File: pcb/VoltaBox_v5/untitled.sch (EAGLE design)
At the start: 46 parts, among them J1 1050170001, Q1 8 MHz, Q2 32768Hz, U1 MCU-STM32F103RCT6(LQFP64), U2 ADUM1401WTRWZ, U4 LMP92064SD/NOPB, X1 112J-TDAR-R(MICROSD)

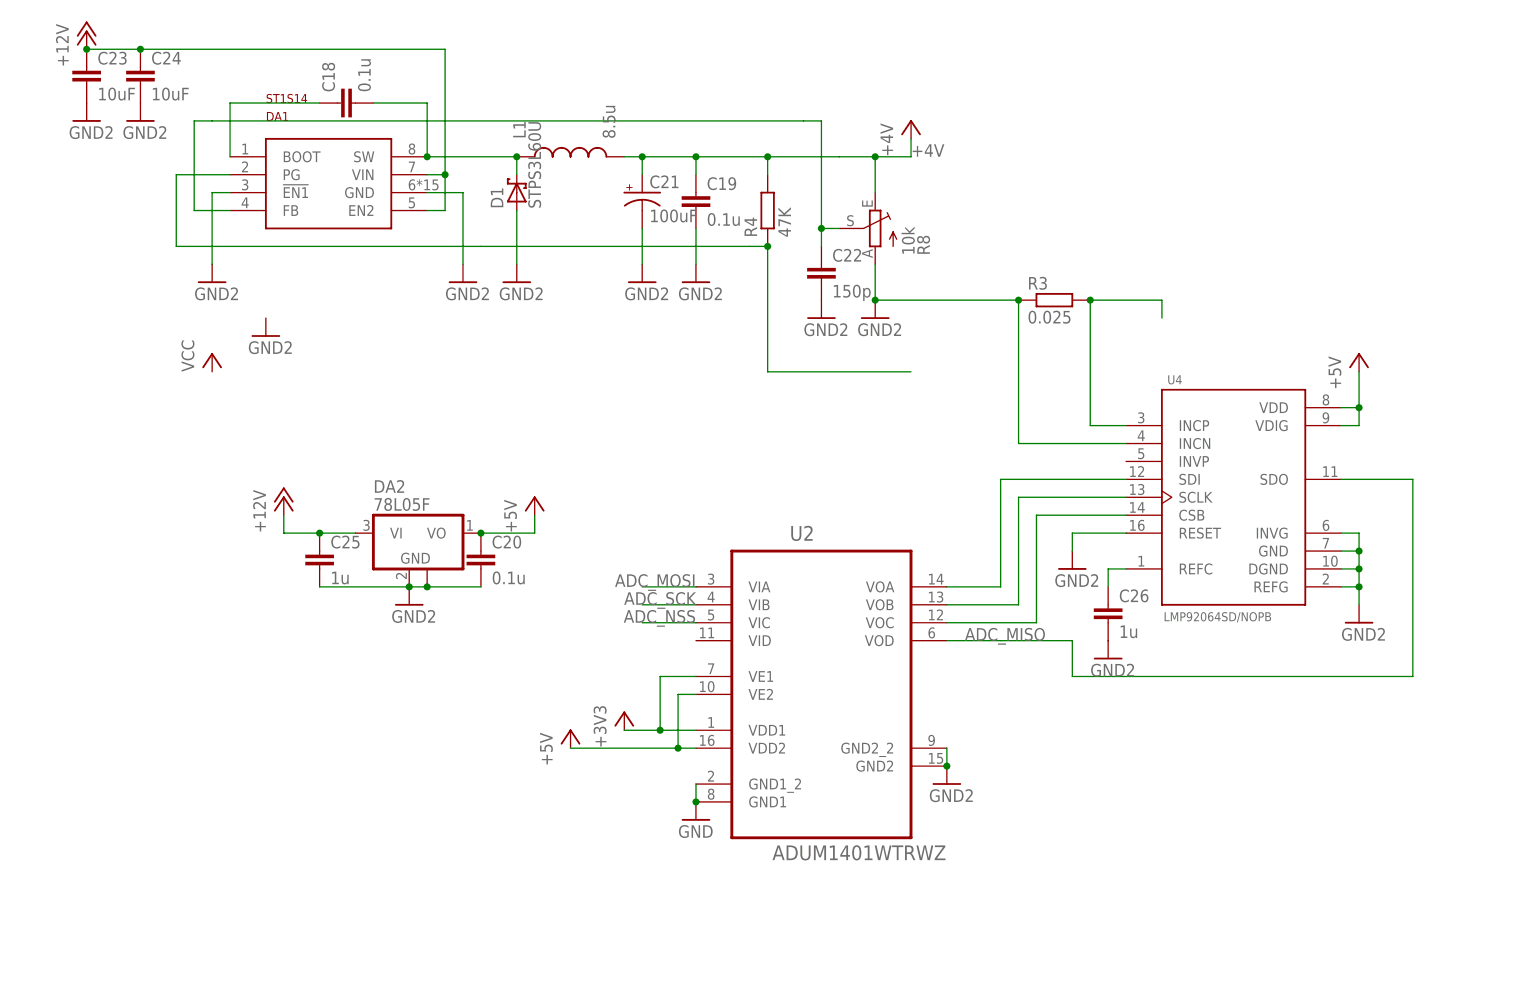
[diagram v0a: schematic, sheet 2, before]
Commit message: Some PCB changes. ICs prefix changes. Added some capacitors. Q3 case type changed.
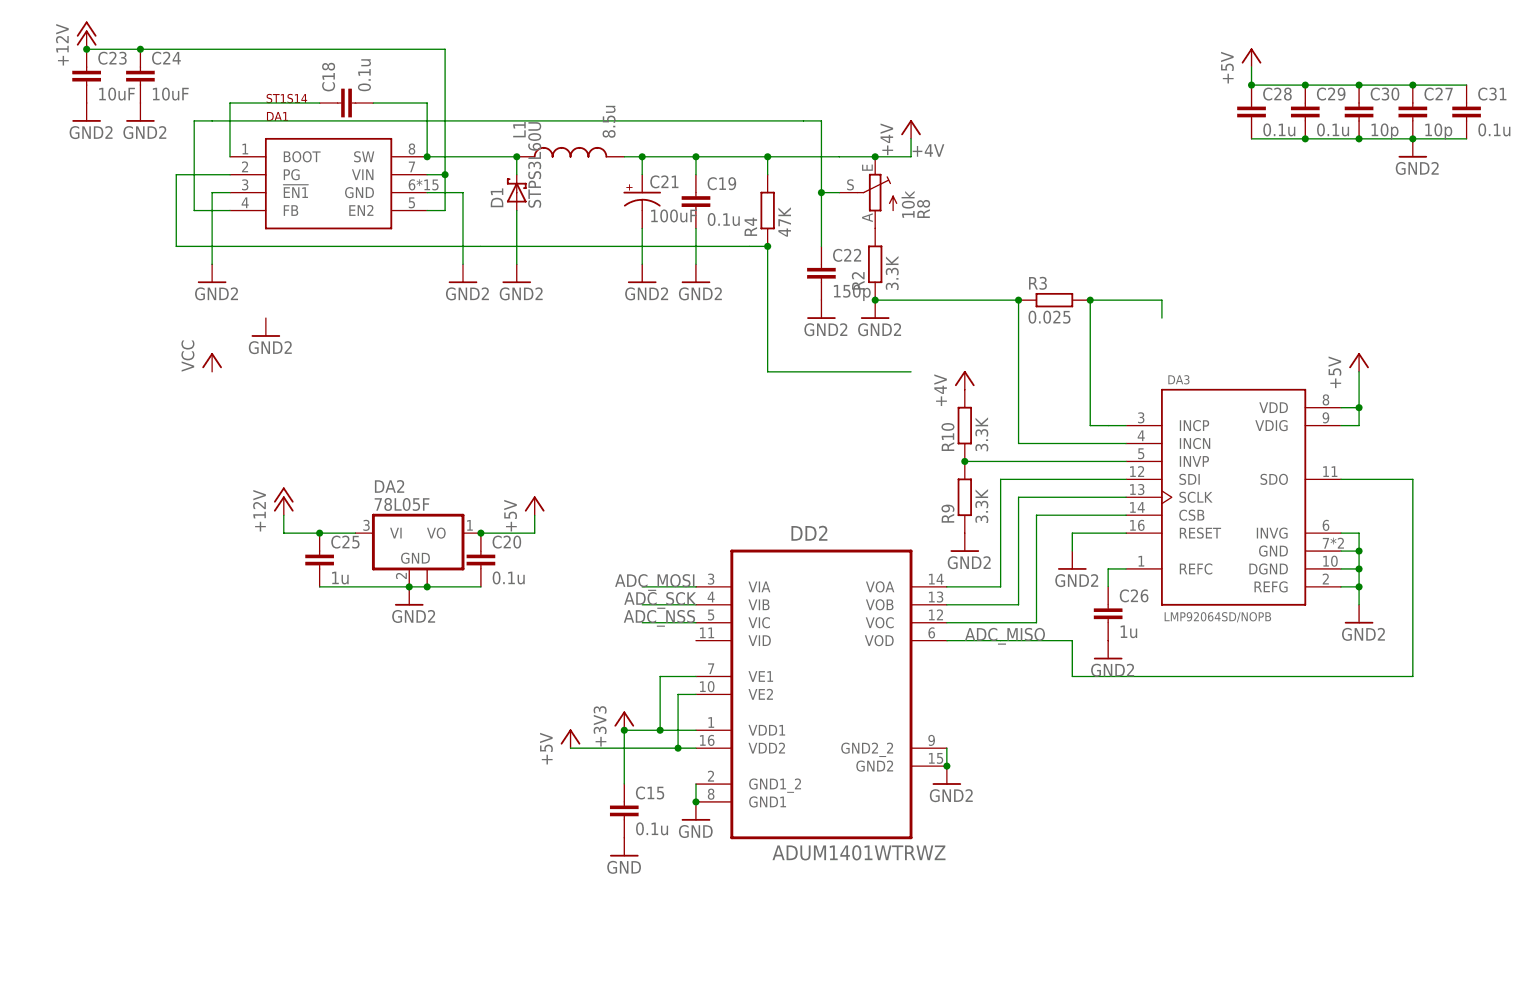
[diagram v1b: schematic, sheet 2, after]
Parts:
- removed Q2: 32768Hz, crystal:FC-12M
- removed U4: LMP92064SD/NOPB, LMP92064SD_NOPB:LMP92064SD/NOPB
- added C15, C28, C29, C31: 0.1u, eagle-ltspice:CC0603
- added C27, C30: 10p, eagle-ltspice:CC0603
- added DA4: (no value), SparkFun-IC-Power:V_REG_LM1117SOT223
- added Q3: 8MHz, crystal:CRYSTALHC49UP
- added R10, R2, R9: 3.3K, resistor:R-EU_R0603
- DA3: value (none) -> LMP92064SD/NOPB; device SparkFun-IC-Power:V_REG_LM1117SOT223 -> LMP92064SD_NOPB:LMP92064SD/NOPB
- Q1: value 8 MHz -> 32768Hz; device crystal-geyer_V1_0:KX-7 -> crystal-geyer_V1_0:KX-327-NHT
- renumbered U1 to DD1, U2 to DD2
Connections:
- new net N$24: R2.2, R8.A
- new net N$25: DA3.INVP, R10.1, R9.2
- net +3V3: now also C15.1, DA4.OUT, DA4.OUT@1; no longer DA3.OUT, DA3.OUT@1
- net +4V: now also R10.2
- net +5V: now also C27.1, C28.1, C29.1, C30.1, C31.1, DA3.VDD, DA3.VDIG; no longer U4.VDD, U4.VDIG
- net ADC_MISO: now also DA3.SDO; no longer U4.SDO
- net GND: now also C15.2, C27.2, C28.2, C29.2, C30.2, C31.2, DA3.DGND, DA3.GND, DA3.INCN, DA3.INVG, DA3.REFG, DA3.RESET, DA4.ADJ, R2.1, R9.1; no longer DA3.ADJ, R8.A, U4.DGND, U4.GND, U4.INCN, U4.INVG, U4.REFG, U4.RESET
- net N$1: now also Q3.1; no longer Q1.1
- net N$11: now also DA3.SDI; no longer U4.SDI
- net N$2: now also Q3.2; no longer Q1.2
- net N$23: now also DA3.INCP; no longer U4.INCP
- net N$3: now also DA3.REFC; no longer U4.REFC
- net N$5: now also DA3.SCLK; no longer U4.SCLK
- net N$6: now also DA3.CSB; no longer U4.CSB
- net N$7: now also Q1.2; no longer Q2.2
- net N$8: now also Q1.1; no longer Q2.1
- net VCC: now also DA4.IN; no longer DA3.IN
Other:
- moved on the sheet: Q1, R8

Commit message: DC-DC new layout, adc part implemented
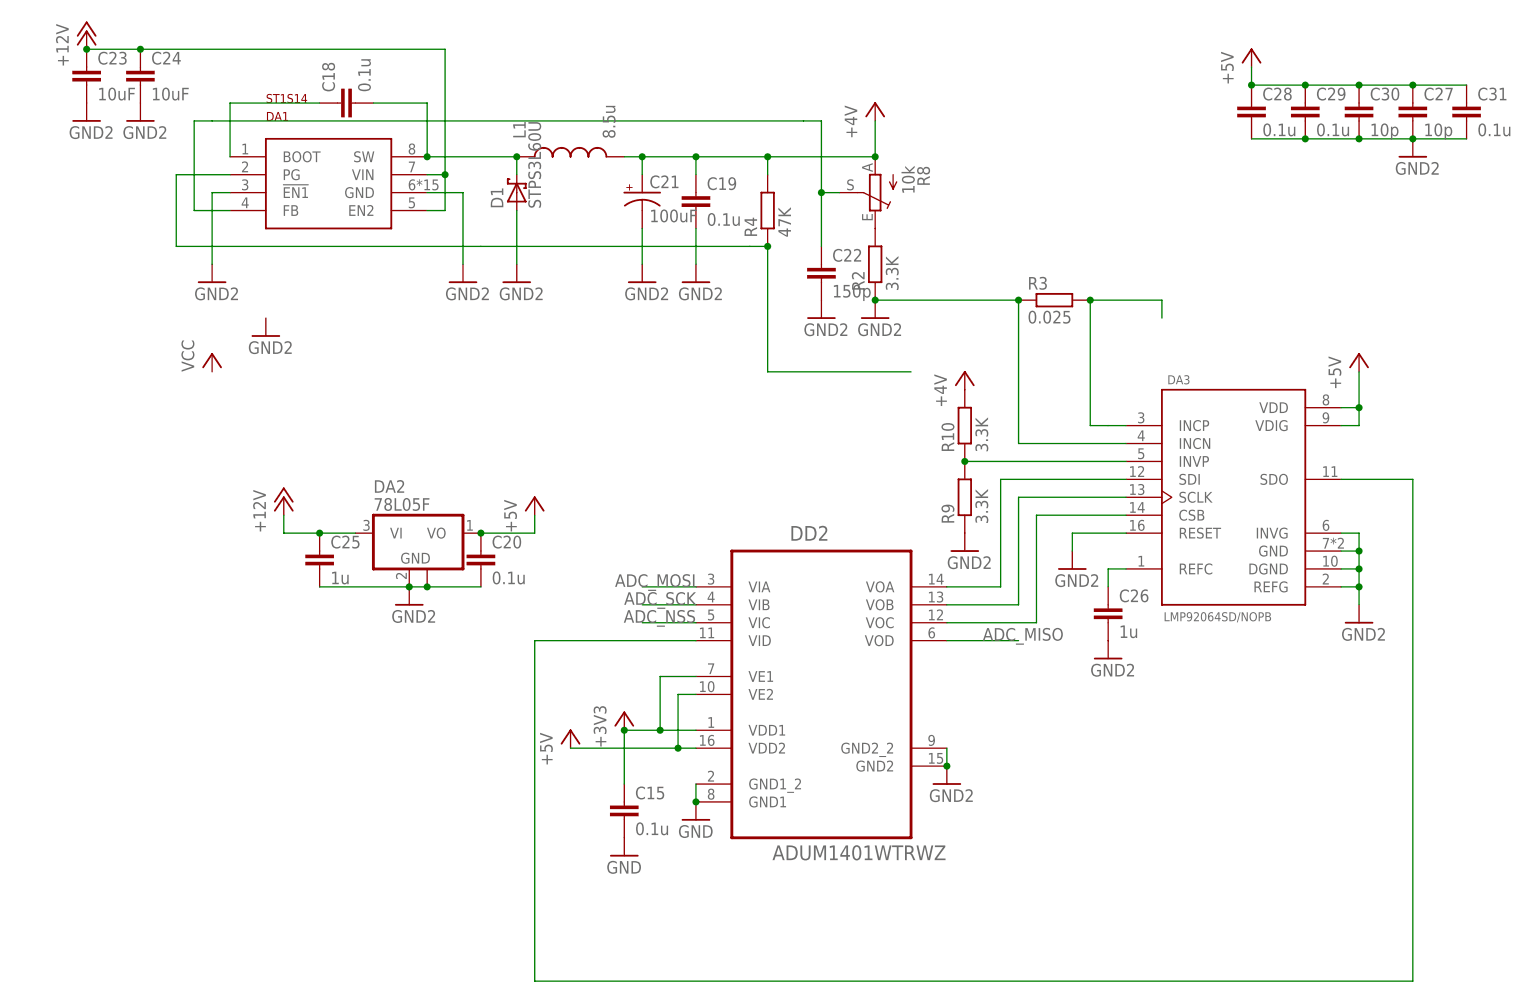
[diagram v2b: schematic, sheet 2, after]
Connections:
- removed net N$24: R2.2, R8.A
- new net N$22: R2.2, R8.E
- new net N$26: DA3.SDO, DD2.VID
- net +4V: now also R8.A; no longer R8.E
- net ADC_MISO: no longer DA3.SDO
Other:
- moved on the sheet: R8
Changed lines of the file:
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@@
 <instance part="U$10" gate="G$1" x="15.24" y="5.08"/>
 <instance part="R4" gate="G$1" x="86.36" y="22.86" rot="R90"/>
-<instance part="R8" gate="1" x="101.6" y="25.4" rot="MR0"/>
+<instance part="R8" gate="1" x="101.6" y="25.4" rot="R180"/>
 <instance part="DA3" gate="G$1" x="152.4" y="-17.78"/>
 <instance part="R3" gate="G$1" x="127" y="10.16"/>
-<instance part="U$12" gate="G$1" x="106.68" y="35.56"/>
+<instance part="U$12" gate="G$1" x="101.6" y="38.1"/>
 <instance part="U$11" gate="G$1" x="170.18" y="-35.56"/>
 <instance part="DA2" gate="G$1" x="35.56" y="-22.86"/>
@@
 <net name="+4V" class="0">
 <segment>
+<pinref part="U$19" gate="G$1" pin="+4V"/>
+<pinref part="R10" gate="G$1" pin="2"/>
+</segment>
+<segment>
 <pinref part="L1" gate="G$1" pin="2"/>
 <wire x1="66.04" y1="30.48" x2="68.58" y2="30.48" width="0.1524" layer="91"/>
@@
 <wire x1="76.2" y1="30.48" x2="86.36" y2="30.48" width="0.1524" layer="91"/>
 <pinref part="C21" gate="G$1" pin="+"/>
-<wire x1="86.36" y1="30.48" x2="96.52" y2="30.48" width="0.1524" layer="91"/>
 <wire x1="68.58" y1="27.94" x2="68.58" y2="30.48" width="0.1524" layer="91"/>
 <junction x="68.58" y="30.48"/>
 <pinref part="R4" gate="G$1" pin="2"/>
 <wire x1="86.36" y1="27.94" x2="86.36" y2="30.48" width="0.1524" layer="91"/>
+<pinref part="R8" gate="1" pin="A"/>
+<wire x1="86.36" y1="30.48" x2="101.6" y2="30.48" width="0.1524" layer="91"/>
 <junction x="86.36" y="30.48"/>
-<pinref part="R8" gate="1" pin="E"/>
-<wire x1="101.6" y1="30.48" x2="96.52" y2="30.48" width="0.1524" layer="91"/>
-<label x="106.68" y="30.48" size="1.778" layer="95"/>
+<pinref part="U$12" gate="G$1" pin="+4V"/>
+<wire x1="101.6" y1="30.48" x2="101.6" y2="35.56" width="0.1524" layer="91"/>
 <junction x="101.6" y="30.48"/>
-<pinref part="U$12" gate="G$1" pin="+4V"/>
-<wire x1="101.6" y1="30.48" x2="106.68" y2="30.48" width="0.1524" layer="91"/>
-<wire x1="106.68" y1="30.48" x2="106.68" y2="33.02" width="0.1524" layer="91"/>
-</segment>
-<segment>
-<pinref part="U$19" gate="G$1" pin="+4V"/>
-<pinref part="R10" gate="G$1" pin="2"/>
 </segment>
 </net>
@@
 <net name="ADC_MISO" class="0">
 <segment>
-<wire x1="111.76" y1="-38.1" x2="119.38" y2="-38.1" width="0.1524" layer="91"/>
-<label x="114.3" y="-38.1" size="1.778" layer="95"/>
+<wire x1="111.76" y1="-38.1" x2="121.92" y2="-38.1" width="0.1524" layer="91"/>
+<label x="116.84" y="-38.1" size="1.778" layer="95"/>
 <pinref part="DD2" gate="A" pin="VOD"/>
-<wire x1="119.38" y1="-38.1" x2="129.54" y2="-38.1" width="0.1524" layer="91"/>
-<wire x1="129.54" y1="-38.1" x2="129.54" y2="-43.18" width="0.1524" layer="91"/>
-<wire x1="129.54" y1="-43.18" x2="177.8" y2="-43.18" width="0.1524" layer="91"/>
-<wire x1="177.8" y1="-43.18" x2="177.8" y2="-15.24" width="0.1524" layer="91"/>
-<pinref part="DA3" gate="G$1" pin="SDO"/>
-<wire x1="177.8" y1="-15.24" x2="167.64" y2="-15.24" width="0.1524" layer="91"/>
 </segment>
 </net>
@@
 </segment>
 </net>
-<net name="N$24" class="0">
-<segment>
-<pinref part="R8" gate="1" pin="A"/>
-<pinref part="R2" gate="G$1" pin="2"/>
-</segment>
-</net>
 <net name="N$25" class="0">
 <segment>
@@
 </segment>
 </net>
+<net name="N$26" class="0">
+<segment>
+<pinref part="DA3" gate="G$1" pin="SDO"/>
+<wire x1="167.64" y1="-15.24" x2="177.8" y2="-15.24" width="0.1524" layer="91"/>
+<wire x1="177.8" y1="-15.24" x2="177.8" y2="-86.36" width="0.1524" layer="91"/>
+<wire x1="177.8" y1="-86.36" x2="53.34" y2="-86.36" width="0.1524" layer="91"/>
+<wire x1="53.34" y1="-86.36" x2="53.34" y2="-38.1" width="0.1524" layer="91"/>
+<pinref part="DD2" gate="A" pin="VID"/>
+<wire x1="53.34" y1="-38.1" x2="76.2" y2="-38.1" width="0.1524" layer="91"/>
+</segment>
+</net>
+<net name="N$22" class="0">
+<segment>
+<pinref part="R2" gate="G$1" pin="2"/>
+<pinref part="R8" gate="1" pin="E"/>
+</segment>
+</net>
